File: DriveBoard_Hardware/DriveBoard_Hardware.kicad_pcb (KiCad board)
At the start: 2 copper layers, 61 x 99.8 mm, 30 parts, among them U1 MAX_3232, U2 MAX_3232, U3 AP1059, U4 TM4C129E_Launchpad

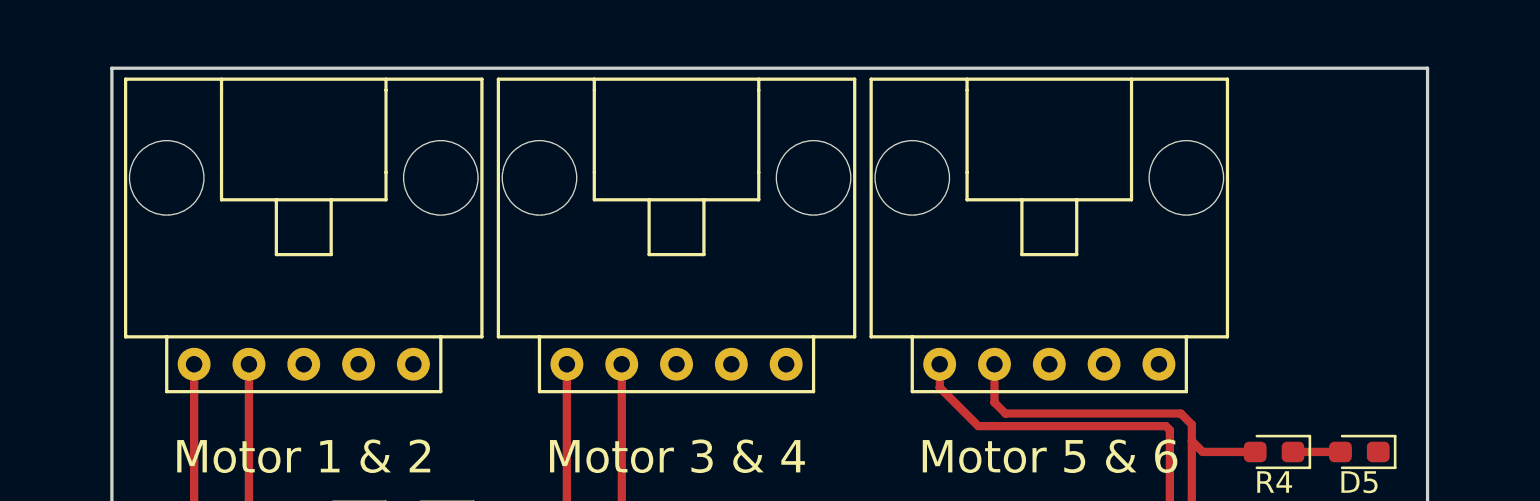
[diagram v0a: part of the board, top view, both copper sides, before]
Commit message: Updated to using buttons/switch
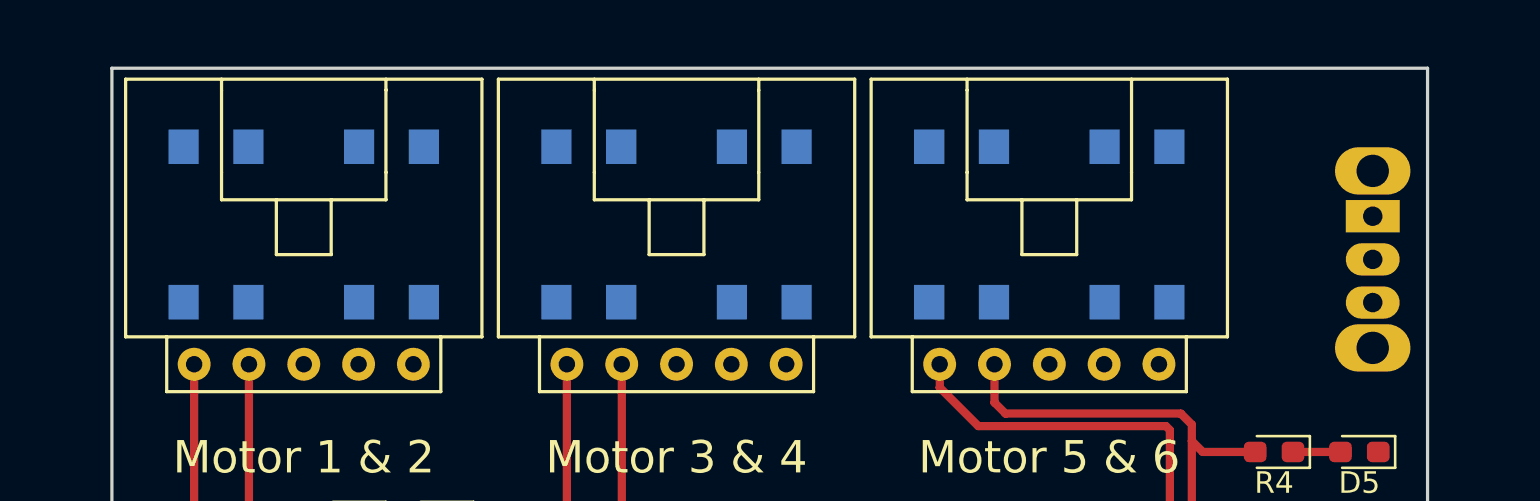
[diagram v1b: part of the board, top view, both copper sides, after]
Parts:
- added SW1: SW_Push, Button_Switch_SMD:SW_SPST_TL3305A, B.Cu at (127.3, 42.5)
- added SW2: SW_Push, Button_Switch_SMD:SW_SPST_TL3305A, B.Cu at (135.4, 42.5)
- added SW3: SW_Push, Button_Switch_SMD:SW_SPST_TL3305A, B.Cu at (144.5, 42.5)
- added SW4: SW_Push, Button_Switch_SMD:SW_SPST_TL3305A, B.Cu at (152.7, 42.5)
- added SW5: SW_Push, Button_Switch_SMD:SW_SPST_TL3305A, B.Cu at (161.8, 42.5)
- added SW6: SW_Push, Button_Switch_SMD:SW_SPST_TL3305A, B.Cu at (169.9, 42.5)
- added SW7: SW_SPDT, Button_Switch_THT:SW_CuK_OS102011MA1QN1_SPDT_Angled, B.Cu at (180.8, 42.2)
- Conn2, Conn3, Conn4: footprint MRDT_Connectors:MOLEX_SL_05_Horizontal -> DriveBoard_Hardware:MOLEX_SL_05_Horizontal_NoMountingHole
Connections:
- U4 pad PD2: Net-(U4-PadPD2) -> DIRECTION_SW
- U4 pad PD4: Net-(U4-PadPD4) -> M1_SW
- U4 pad PD5: Net-(U4-PadPD5) -> M2_SW
- U4 pad PN4: Net-(U4-PadPN4) -> M6_SW
- U4 pad PN5: Net-(U4-PadPN5) -> M5_SW
- U4 pad PP4: Net-(U4-PadPP4) -> M4_SW
- U4 pad PQ0: Net-(U4-PadPQ0) -> M3_SW
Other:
- board text added: "FWD"
- board text added: "M1"
- board text added: "M2"
- board text added: "M3"
- board text added: "M4"
- board text added: "M5"
- board text added: "M6"
- board text added: "REV"

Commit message: changes to schematic and starting changes to layout
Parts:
- added D6: LED, LED_SMD:LED_0603_1608Metric_Pad1.05x0.95mm_HandSolder, F.Cu at (208.5, 36.9)
- added D7: LED, LED_SMD:LED_0603_1608Metric_Pad1.05x0.95mm_HandSolder, F.Cu at (208.5, 38.5)
- added D8: LED, LED_SMD:LED_0603_1608Metric_Pad1.05x0.95mm_HandSolder, F.Cu at (211.9, 36.9)
- added D9: LED, LED_SMD:LED_0603_1608Metric_Pad1.05x0.95mm_HandSolder, F.Cu at (208.5, 40.0)
- added R5: 500, LED_SMD:LED_0603_1608Metric_Pad1.05x0.95mm_HandSolder, F.Cu at (211.9, 38.5)
- added R6: 500, LED_SMD:LED_0603_1608Metric_Pad1.05x0.95mm_HandSolder, F.Cu at (215.3, 36.9)
- added R7: 500, LED_SMD:LED_0603_1608Metric_Pad1.05x0.95mm_HandSolder, F.Cu at (211.9, 40.0)
- added R8: 500, LED_SMD:LED_0603_1608Metric_Pad1.05x0.95mm_HandSolder, F.Cu at (215.3, 38.5)
- C3, C4, C5, C6: value .1uF -> 10uF
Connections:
- C1 pad 1: +3V3 -> GND
- C1 pad 2: GND -> +5V
- C2 pad 1: +3V3 -> GND
- C2 pad 2: GND -> +5V
- C8 pad 1: +3V3 -> +5V
- L1 pad 2: +3V3 -> +5V
- R1 pad 2: +3V3 -> +5V
- SW1 pad 1: +3V3 -> +5V
- SW2 pad 1: +3V3 -> +5V
- SW3 pad 1: +3V3 -> +5V
- SW4 pad 1: +3V3 -> +5V
- SW5 pad 1: +3V3 -> +5V
- SW6 pad 1: +3V3 -> +5V
- SW7 pad 2: +3V3 -> +5V
- U1 pad 1: Net-(C9-Pad1) -> Net-(C9-Pad2)
- U1 pad 16: +3V3 -> +5V
- U1 pad 3: Net-(C9-Pad2) -> Net-(C9-Pad1)
- U1 pad 4: Net-(C10-Pad1) -> Net-(C10-Pad2)
- U1 pad 5: Net-(C10-Pad2) -> Net-(C10-Pad1)
- U2 pad 1: Net-(C11-Pad1) -> Net-(C11-Pad2)
- U2 pad 16: +3V3 -> +5V
- U2 pad 3: Net-(C11-Pad2) -> Net-(C11-Pad1)
- U2 pad 4: Net-(C12-Pad1) -> Net-(C12-Pad2)
- U2 pad 5: Net-(C12-Pad2) -> Net-(C12-Pad1)
- U3 pad 3: +3V3 -> +5V
- U4 pad +3V3: +3V3 -> Net-(U4-Pad+3V3)
- U4 pad +5V: Net-(U4-Pad+5V) -> +5V
- U4 pad PB4: Net-(U4-PadPB4) -> Power
- U4 pad PB5: Net-(U4-PadPB5) -> Watchdog
- U4 pad PD4: M1_SW -> Rspeed
- U4 pad PD5: M2_SW -> Lspeed
- U4 pad PK2: Net-(U4-PadPK2) -> M1_SW
- U4 pad PK3: Net-(U4-PadPK3) -> M2_SW
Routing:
- net +5V: track 0.00 -> 76.8 mm, vias 0 -> 1
- net +3V3: track 151.0 -> 83.0 mm, vias 5 -> 2

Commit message: making changes
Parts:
- removed D1: D_Schottky, Diode_SMD:D_0603_1608Metric_Pad1.05x0.95mm_HandSolder
- removed L1: 47uH, Inductor_SMD:L_0603_1608Metric_Pad1.05x0.95mm_HandSolder
- U3: value AP1059 -> OKI; footprint Package_SO:SOIC-8_3.9x4.9mm_P1.27mm -> MRDT_Devices:OKI_Horizontal
- moved R8 98.9 mm to (136.7, 98.7), turned to 270 degrees
- moved R6 93.5 mm to (145.0, 98.7), turned to 270 degrees
- moved R7 91.9 mm to (141.0, 98.6), turned to 270 degrees
- moved D8 91.5 mm to (141.0, 94.7), turned to 270 degrees
- moved D9 90.3 mm to (136.7, 94.9), turned to 270 degrees
- moved R5 86.8 mm to (149.4, 98.7), turned to 270 degrees
- moved D7 84.9 mm to (145.0, 94.9), turned to 270 degrees
- moved D6 82.8 mm to (149.4, 94.9), turned to 270 degrees
- moved C1 18.8 mm to (127.5, 83.4), turned to 270 degrees
- moved U3 16.3 mm to (165.9, 88.4), turned to 90 degrees
- moved C4 15.2 mm to (139.4, 76.0), turned to 270 degrees
- moved C3 14.7 mm to (135.6, 86.2), turned to 180 degrees
- moved C9 14.6 mm to (139.4, 83.4), turned to 270 degrees
- moved D2 12.8 mm to (161.0, 84.8), turned to 90 degrees
- moved C10 10.6 mm to (139.4, 79.6), turned to 270 degrees
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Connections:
- U3 pad 2: Net-(D1-Pad1) -> GND
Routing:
- net +5V: track 76.8 -> 310.7 mm, vias 1 -> 2
- net M3_SW: track 0.00 -> 149.1 mm
- net M4_SW: track 0.00 -> 137.9 mm
- net M5_SW: track 0.00 -> 129.5 mm
- net DIRECTION_SW: track 0.00 -> 129.1 mm, vias 0 -> 1
- net M6_SW: track 0.00 -> 119.6 mm
- net +3V3: track 83.0 -> 0.00 mm, vias 2 -> 0
- net M1_SW: track 0.00 -> 75.4 mm
- net M2_SW: track 0.00 -> 73.1 mm
- net /+12V: track 57.4 -> 28.6 mm, vias 2 -> 0
- net RX_1_SL: track 62.6 -> 36.7 mm, vias 0 -> 2
- net TX_1_SL: track 62.7 -> 38.9 mm
- net RX_2_SL: track 54.9 -> 32.3 mm, vias 2 -> 0
- net Lspeed: track 0.00 -> 21.5 mm, vias 0 -> 1
- net Rspeed: track 0.00 -> 19.2 mm, vias 0 -> 1
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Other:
- board size 61 x 99.8 mm -> 61 x 100 mm

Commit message: finishing changes
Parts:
- removed D9: LED, LED_SMD:LED_0603_1608Metric_Pad1.05x0.95mm_HandSolder
- removed R8: 500, LED_SMD:LED_0603_1608Metric_Pad1.05x0.95mm_HandSolder
- added G***: LOGO, MRDT_Silkscreens:MRDT_Logo_10mm, F.Cu at (172.5, 120.1)
- added G***: Eric_Welch_Sig_22mmx9.4mm, DriveBoard_Hardware:Eric_Welch_Sig_22mmx9.4mm, F.Cu at (155.2, 130.0)
- added G***: Jacob_Troy_Sig_22mmx16.5mm, DriveBoard_Hardware:Jacob_Troy_Sig_22mmx16.5mm, F.Cu at (132.3, 129.8)
- moved R1 29.6 mm to (136.9, 98.6), turned to 270 degrees
- moved D2 26.0 mm to (136.9, 94.7), turned to 270 degrees
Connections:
- U4 pad PB4: Power -> Net-(U4-PadPB4)
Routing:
- net Power: track 15.7 -> 0.00 mm, vias 1 -> 0
- net +5V: track 310.7 -> 325.2 mm, vias 2 -> 1
- net Net-(D9-Pad2): track 2.02 -> 0.00 mm
- net RX_2_IC: track 36.8 -> 38.1 mm
- net TX_2_IC: track 35.8 -> 36.3 mm
- net GND: vias 2 -> 8
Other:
- board text added: "5V"
- board text added: "Drive Board, Rev.1 Mars Rover Design Team Missouri S&T, 2019 Jacob Troy & Eric Welch"
- board text added: "Lspeed"
- board text added: "Power"
- board text added: "Rspeed"
- board text added: "TX1"
- board text added: "TX2"
- board text added: "TX3"
- board text added: "Watchdog"
- board text removed: "Drive Board Rev.1 Mars Rover Design Team 2019 Missouri S&T Jacob Troy & Eric Welch"

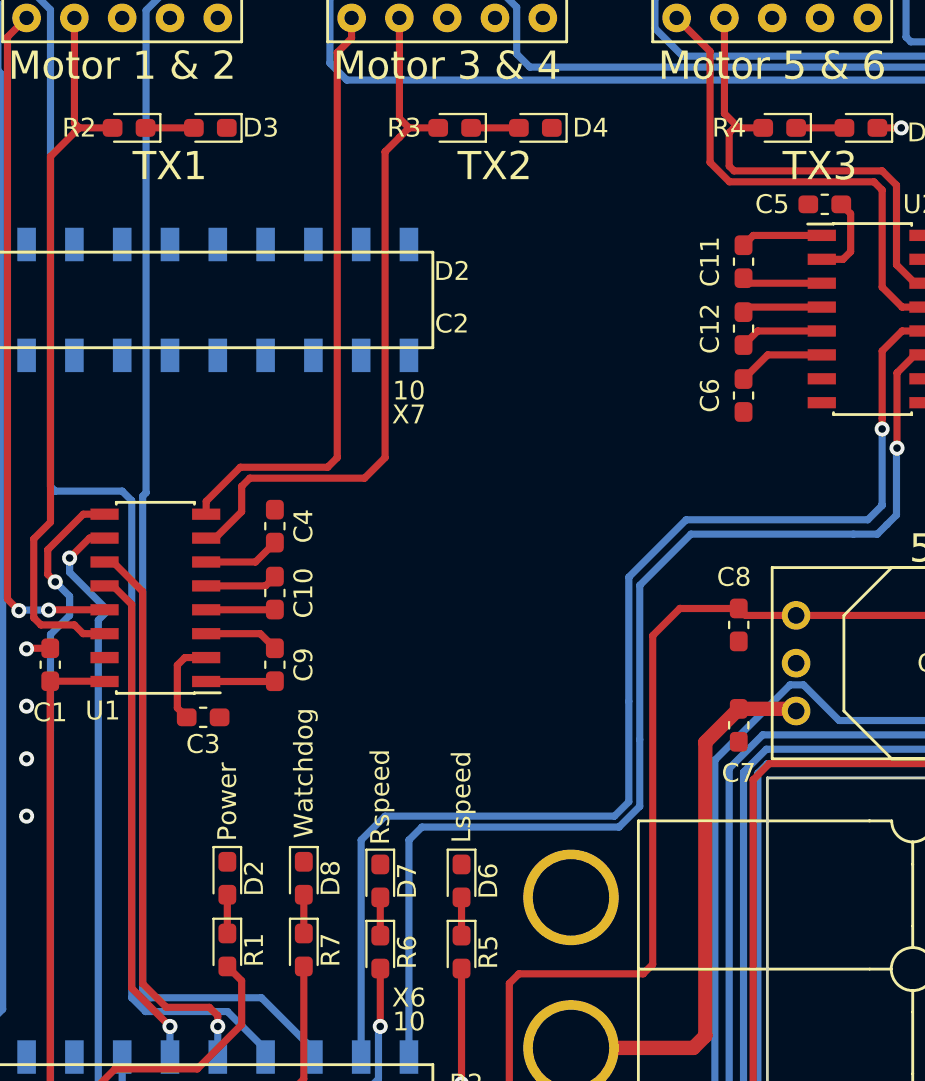
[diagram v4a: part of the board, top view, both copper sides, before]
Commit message: changed BOM
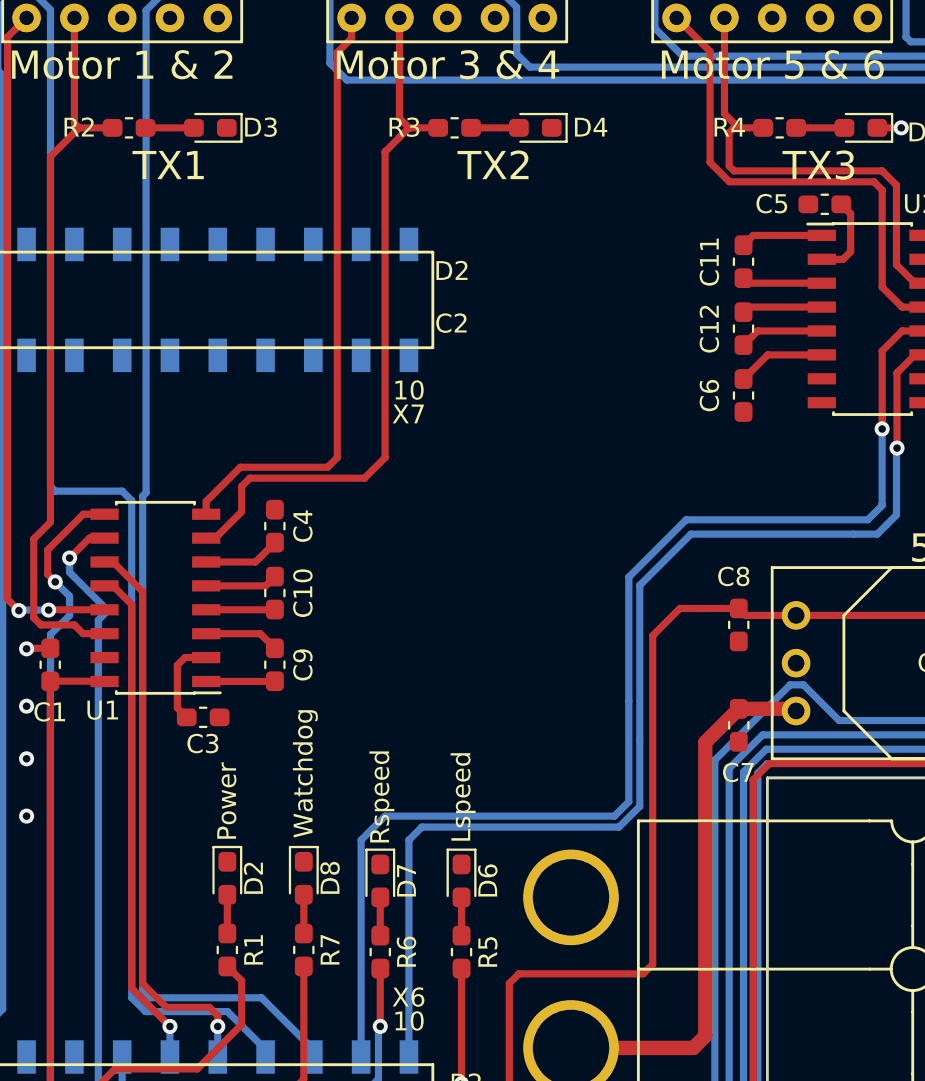
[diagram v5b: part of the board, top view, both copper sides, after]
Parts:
- R1, R2, R3, R4, R5, R6, R7: footprint LED_SMD:LED_0603_1608Metric_Pad1.05x0.95mm_HandSolder -> Resistor_SMD:R_0603_1608Metric_Pad1.05x0.95mm_HandSolder

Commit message: updating changes (Rev1 Review)
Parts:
- added R10: 10K, Resistor_SMD:R_0603_1608Metric_Pad1.05x0.95mm_HandSolder, B.Cu at (140.0, 41.8)
- added R11: 10K, Resistor_SMD:R_0603_1608Metric_Pad1.05x0.95mm_HandSolder, B.Cu at (148.6, 42.0)
- added R12: 10K, Resistor_SMD:R_0603_1608Metric_Pad1.05x0.95mm_HandSolder, B.Cu at (157.7, 42.3)
- added R13: 10K, Resistor_SMD:R_0603_1608Metric_Pad1.05x0.95mm_HandSolder, B.Cu at (165.9, 42.3)
- added R14: 10K, Resistor_SMD:R_0603_1608Metric_Pad1.05x0.95mm_HandSolder, B.Cu at (176.3, 40.0)
- added R8: 10K, Resistor_SMD:R_0603_1608Metric_Pad1.05x0.95mm_HandSolder, B.Cu at (131.6, 45.3)
- added R9: 10K, Resistor_SMD:R_0603_1608Metric_Pad1.05x0.95mm_HandSolder, B.Cu at (131.6, 41.5)
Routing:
- net M1_SW: track 75.4 -> 81.0 mm
- net DIRECTION_SW: track 129.1 -> 134.2 mm
- net M3_SW: track 149.1 -> 152.2 mm
- net M4_SW: track 137.9 -> 140.5 mm
- net M6_SW: track 119.6 -> 122.2 mm
- net M5_SW: track 129.5 -> 132.1 mm
- net M2_SW: track 73.1 -> 75.4 mm
- net GND: vias 8 -> 15
- net +5V: vias 1 -> 2
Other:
- board size 61 x 100 mm -> 61 x 99.3 mm
- board text added: "-"
- board text added: "Rx"
- board text added: "Tx"

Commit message: updated Rev 2 Libraries
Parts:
- Conn1: footprint MRDT_Connectors:Anderson_2_Horisontal_Side_by_Side -> MRDT_Connectors:Anderson_2_Horizontal_Side_by_Side
- Conn2, Conn3, Conn4: footprint DriveBoard_Hardware:MOLEX_SL_05_Horizontal_NoMountingHole -> MRDT_Connectors:MOLEX_SL_05_Horizontal
- R1, R2, R3, R4, R5, R6, R7: footprint Resistor_SMD:R_0603_1608Metric_Pad1.05x0.95mm_HandSolder -> LED_SMD:LED_0603_1608Metric_Pad1.05x0.95mm_HandSolder
- U4: footprint MRDT_Shields:TM4C129E_Launchpad_X7_Bottom_SMD -> MRDT_Shields:TM4C129E_Launchpad_X7_SMD_BOTTOM
- moved C7 1.02 mm to (164.1, 85.6)
- moved U3 1.02 mm to (165.9, 87.4)
- moved C8 0.65 mm to (164.1, 80.6)
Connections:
- SW7 pad 3: Net-(SW7-Pad3) -> (no net)
- U2 pad 10: Net-(U2-Pad10) -> (no net)
- U2 pad 7: Net-(U2-Pad7) -> (no net)
- U2 pad 8: Net-(U2-Pad8) -> (no net)
- U2 pad 9: Net-(U2-Pad9) -> (no net)
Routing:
- net +5V: track 325.2 -> 327.9 mm
- net M3_SW: track 152.2 -> 154.9 mm
- net /+12V: track 28.6 -> 26.2 mm

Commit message: Created rev 2
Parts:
- removed C10, C11, C12, C9: .1uF, Capacitor_SMD:C_0603_1608Metric_Pad1.05x0.95mm_HandSolder
- removed C4, C5, C6: 10uF, Capacitor_SMD:C_0603_1608Metric_Pad1.05x0.95mm_HandSolder
- removed the G*** at (172.5, 120.1)
- removed the G*** at (155.2, 130.0)
- removed the G*** at (132.3, 129.8)
- added Conn5: Molex_SL_03, MRDT_Connectors:MOLEX_SL_03_Horizontal, B.Cu at (78.7, 84.6)
- added Conn6: Molex_SL_03, MRDT_Connectors:MOLEX_SL_03_Horizontal, B.Cu at (96.5, 84.6)
- added Conn7: Molex_SL_03, MRDT_Connectors:MOLEX_SL_03_Horizontal, B.Cu at (114.3, 84.6)
- added D1: LED, LED_SMD:LED_0603_1608Metric_Pad1.05x0.95mm_HandSolder, F.Cu at (73.7, 90.0)
- added D10: LED, LED_SMD:LED_0603_1608Metric_Pad1.05x0.95mm_HandSolder, F.Cu at (109.2, 90.1)
- added D11: LED, LED_SMD:LED_0603_1608Metric_Pad1.05x0.95mm_HandSolder, F.Cu at (78.7, 108.3)
- added D12: LED, LED_SMD:LED_0603_1608Metric_Pad1.05x0.95mm_HandSolder, F.Cu at (86.4, 108.3)
- added D13: LED, LED_SMD:LED_0603_1608Metric_Pad1.05x0.95mm_HandSolder, F.Cu at (94.0, 108.3)
- added D14: LED, LED_SMD:LED_0603_1608Metric_Pad1.05x0.95mm_HandSolder, F.Cu at (101.6, 108.3)
- added D15: LED, LED_SMD:LED_0603_1608Metric_Pad1.05x0.95mm_HandSolder, F.Cu at (109.2, 108.3)
- added D16: LED, LED_SMD:LED_0603_1608Metric_Pad1.05x0.95mm_HandSolder, F.Cu at (116.8, 108.3)
- added D17: LED, LED_SMD:LED_0603_1608Metric_Pad1.05x0.95mm_HandSolder, F.Cu at (124.9, 99.8)
- added D9: LED, LED_SMD:LED_0603_1608Metric_Pad1.05x0.95mm_HandSolder, F.Cu at (91.4, 90.1)
- added G***: LOGO, MRDT_Silkscreens:z_sig_Andrew_Van_Horn_Sig_15mm, F.Cu at (80.0, 156.2)
- added G***: LOGO, MRDT_Silkscreens:2_Dahlbot_2.0, F.Cu at (122.6, 154.9)
- added R15: 500, LED_SMD:LED_0603_1608Metric_Pad1.05x0.95mm_HandSolder, F.Cu at (73.7, 94.3)
- added R16: 500, LED_SMD:LED_0603_1608Metric_Pad1.05x0.95mm_HandSolder, F.Cu at (91.4, 94.3)
- added R17: 500, LED_SMD:LED_0603_1608Metric_Pad1.05x0.95mm_HandSolder, F.Cu at (109.2, 94.3)
- added U5: MAX3077E, Package_SO:SOIC-8_3.9x4.9mm_P1.27mm, F.Cu at (114.3, 92.2)
- C1, C2: value .1uF -> 10u
- C3: value 10uF -> 10u
- R10, R11, R12, R13, R14, R8, R9, SW1, SW2, SW3, SW4, SW5, SW6, SW7: moved to F.Cu
- U1, U2: value MAX_3232 -> MAX3077E; footprint Package_SO:SOIC-16_3.9x9.9mm_P1.27mm -> Package_SO:SOIC-8_3.9x4.9mm_P1.27mm
- moved C2 102.3 mm to (97.8, 126.1)
- moved SW7 85.9 mm to (127.0, 109.2), turned to 90 degrees
- moved R5 81.5 mm to (72.4, 125.6)
- moved D6 81.5 mm to (72.4, 121.8)
- moved SW6 81.2 mm to (120.9, 107.2), turned to 270 degrees
- moved SW5 80.9 mm to (113.3, 107.2), turned to 270 degrees
- moved SW4 80.0 mm to (105.6, 107.2), turned to 270 degrees
- moved SW3 79.7 mm to (98.0, 107.2), turned to 270 degrees
- moved U2 79.5 mm to (96.5, 92.2), turned to 90 degrees
- moved R8 79.3 mm to (78.7, 104.5), turned to 90 degrees
- moved R13 79.2 mm to (116.8, 104.5)
- moved R12 78.9 mm to (109.2, 104.5)
- moved SW2 78.8 mm to (90.4, 107.2), turned to 270 degrees
- moved SW1 78.5 mm to (82.8, 107.2), turned to 270 degrees
- moved R11 78.2 mm to (101.6, 104.5)
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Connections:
- C1 pad 1: GND -> +3V3
- C1 pad 2: +5V -> GND
- C2 pad 1: GND -> +3V3
- C2 pad 2: +5V -> GND
- C3 pad 1: GND -> +3V3
- C3 pad 2: Net-(C3-Pad2) -> GND
- C8 pad 1: +5V -> +3V3
- Conn2 pad 1: RX_1_SL -> A1
- Conn2 pad 2: TX_1_SL -> B1
- Conn2 pad 3: Net-(Conn2-Pad3) -> GND
- Conn2 pad 4: Net-(Conn2-Pad4) -> Z1
- Conn2 pad 5: GND -> Y1
- Conn3 pad 1: RX_2_SL -> A2
- Conn3 pad 2: TX_2_SL -> B2
- Conn3 pad 3: Net-(Conn3-Pad3) -> GND
- Conn3 pad 4: Net-(Conn3-Pad4) -> Z2
- Conn3 pad 5: GND -> Y2
- Conn4 pad 1: RX_3_SL -> A3
- Conn4 pad 2: TX_3_SL -> B3
- Conn4 pad 3: Net-(Conn4-Pad3) -> GND
- Conn4 pad 4: Net-(Conn4-Pad4) -> Z3
- Conn4 pad 5: GND -> Y3
- R1 pad 2: +5V -> +3V3
- R10 pad 1: GND -> Net-(D13-Pad2)
- R11 pad 1: GND -> Net-(D14-Pad2)
- R12 pad 1: GND -> Net-(D15-Pad2)
- R13 pad 1: GND -> Net-(D16-Pad2)
- R14 pad 1: GND -> Net-(D17-Pad2)
- R2 pad 2: TX_1_SL -> TX_1
- R3 pad 2: TX_2_SL -> TX_2
- R4 pad 2: TX_3_SL -> TX_3
- R8 pad 1: GND -> Net-(D11-Pad2)
- R9 pad 1: GND -> Net-(D12-Pad2)
- SW1 pad 1: +5V -> +3V3
- SW2 pad 1: +5V -> +3V3
- SW3 pad 1: +5V -> +3V3
- SW4 pad 1: +5V -> +3V3
- SW5 pad 1: +5V -> +3V3
- SW6 pad 1: +5V -> +3V3
- SW7 pad 1: DIRECTION_SW -> Net-(SW7-Pad1)
- SW7 pad 2: +5V -> +3V3
- SW7 pad 3: (no net) -> DIRECTION_SW
- U1 pad 1: Net-(C9-Pad2) -> +3V3
- U1 pad 2: Net-(C3-Pad2) -> RX_1
- U1 pad 3: Net-(C9-Pad1) -> TX_1
- U1 pad 4: Net-(C10-Pad2) -> GND
- U1 pad 5: Net-(C10-Pad1) -> Y1
- U1 pad 6: Net-(C4-Pad2) -> Z1
- U1 pad 7: TX_2_SL -> B1
- U1 pad 8: RX_2_SL -> A1
- U2 pad 1: Net-(C11-Pad2) -> +3V3
- U2 pad 2: Net-(C5-Pad2) -> RX_2
- U2 pad 3: Net-(C11-Pad1) -> TX_2
- U2 pad 4: Net-(C12-Pad2) -> GND
- U2 pad 5: Net-(C12-Pad1) -> Y2
- U2 pad 6: Net-(C6-Pad2) -> Z2
- U2 pad 7: (no net) -> B2
- U2 pad 8: (no net) -> A2
- U3 pad 3: +5V -> +3V3
- U4 pad +3V3': (no net) -> +3V3
- U4 pad +5V': +5V -> Net-(U4-Pad+5V')
- U4 pad PA4: RX_3_IC -> RX_3
- U4 pad PA5: TX_3_IC -> TX_3
- U4 pad PK0: RX_1_IC -> RX_1
- U4 pad PK1: TX_1_IC -> TX_1
- U4 pad PN4: M6_SW -> M3_SW
- U4 pad PN5: M5_SW -> M4_SW
- U4 pad PP0: RX_2_IC -> RX_2
- U4 pad PP1: TX_2_IC -> TX_2
- U4 pad PP4: M4_SW -> M5_SW
- U4 pad PQ0: M3_SW -> M6_SW
- U4 pad Rese': (no net) -> Net-(U4-PadRese')
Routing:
- net +5V: track 327.9 -> 0.00 mm, vias 2 -> 0
- net +3V3: track 0.00 -> 196.4 mm, vias 0 -> 1
- net M3_SW: track 154.9 -> 70.7 mm, vias 0 -> 1
- net RX_2: track 0.00 -> 79.8 mm, vias 0 -> 2
- net TX_2: track 0.00 -> 77.8 mm, vias 0 -> 2
- net RX_3: track 0.00 -> 77.5 mm, vias 0 -> 2
- net TX_3: track 0.00 -> 76.4 mm, vias 0 -> 2
- net M4_SW: track 140.5 -> 68.4 mm, vias 0 -> 1
- net RX_3_IC: track 64.5 -> 0.00 mm, vias 1 -> 0
- net M5_SW: track 132.1 -> 68.5 mm, vias 0 -> 1
- net TX_3_IC: track 60.8 -> 0.00 mm, vias 1 -> 0
- net RX_1: track 0.00 -> 60.2 mm, vias 0 -> 2
- net TX_1: track 0.00 -> 59.9 mm, vias 0 -> 2
- net M1_SW: track 81.0 -> 36.0 mm, vias 0 -> 1
- net M2_SW: track 75.4 -> 31.2 mm, vias 0 -> 1
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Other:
- board size 61 x 99.3 mm -> 61 x 93.6 mm
- board text added: "+"
- board text added: "+3.3V"
- board text added: "3 RS-485 3 UART"
- board text added: "3.3V"
- board text added: "A"
- board text added: "B"
- board text added: "DriveBoard, Rev 2 Mars Rover Sesign Team Missouri S&T, 2019 Andrew Van Horn"
- board text added: "Forward"
- board text added: "Front"
- board text added: "LF"
- board text added: "LM"
- board text added: "LR"
- board text added: "LSpeed"
- board text added: "Middle"
- board text added: "R"
- board text added: "RF"
- board text added: "RM"
- board text added: "RR"
- board text added: "RSpeed"
- board text added: "Rear"
- board text added: "T"
- board text added: "WchDog"
- board text added: "Y"
- board text added: "Z"
- board text removed: "5V"
- board text removed: "Drive Board, Rev.1 Mars Rover Design Team Missouri S&T, 2019 Jacob Troy & Eric Welch"
- board text removed: "FWD"
- board text removed: "Lspeed"
- board text removed: "M1"
- board text removed: "M2"
- board text removed: "M3"
- board text removed: "M4"
- board text removed: "M5"
- board text removed: "M6"
- board text removed: "Motor 1 & 2"
- board text removed: "Motor 3 & 4"
- board text removed: "Motor 5 & 6"
- board text removed: "Power"
- board text removed: "REV"
- board text removed: "Rspeed"
- board text removed: "TX1"
- board text removed: "TX2"
- board text removed: "TX3"
- board text removed: "Watchdog"
